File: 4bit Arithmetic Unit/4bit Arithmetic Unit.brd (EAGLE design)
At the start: 162.5 x 108.9 mm, 100 parts

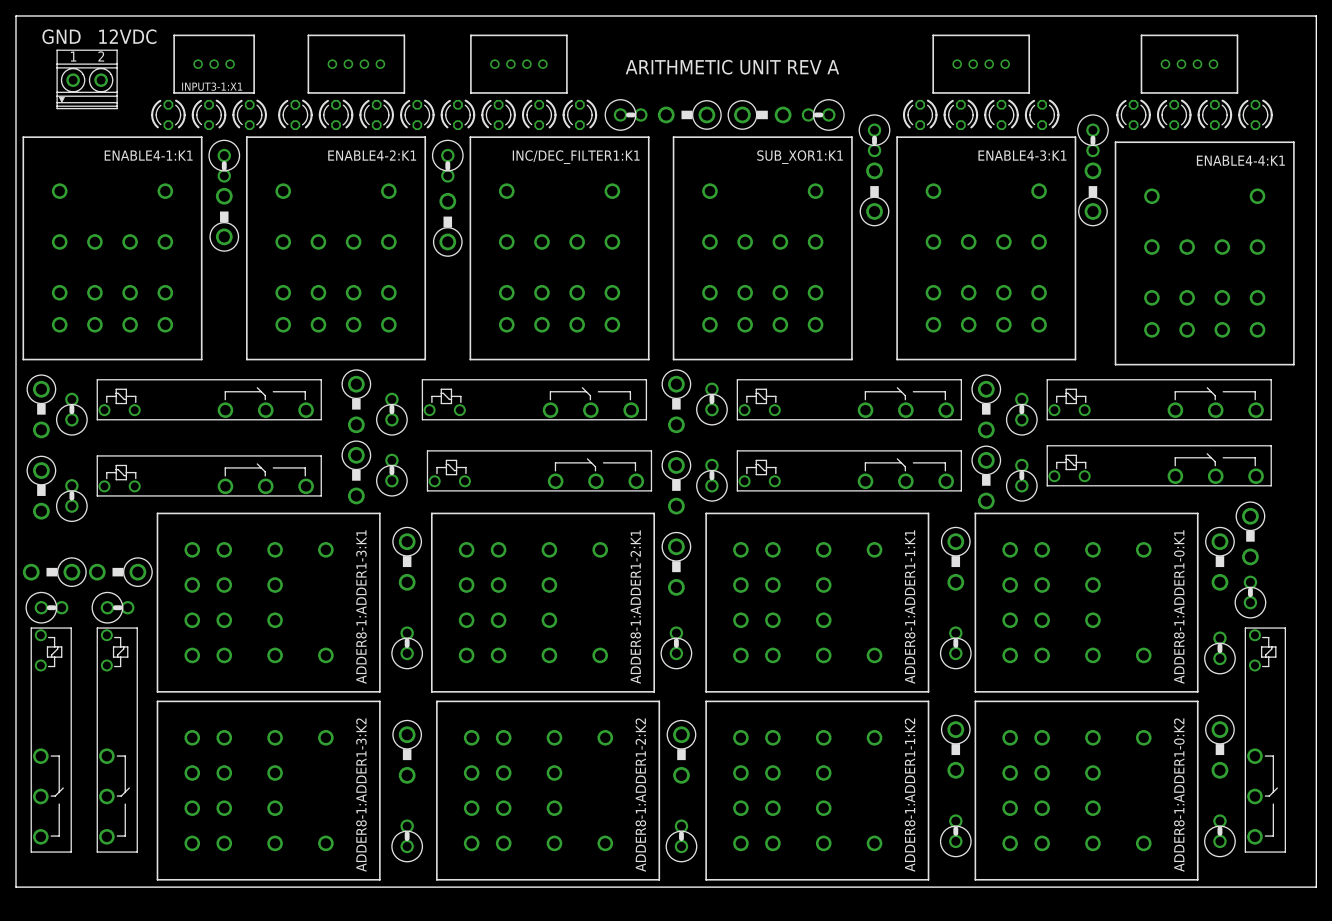
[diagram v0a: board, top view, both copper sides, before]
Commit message: Finishing 4bit AU. Text is actually correct when it appears offset. Worth doing a logical double-check
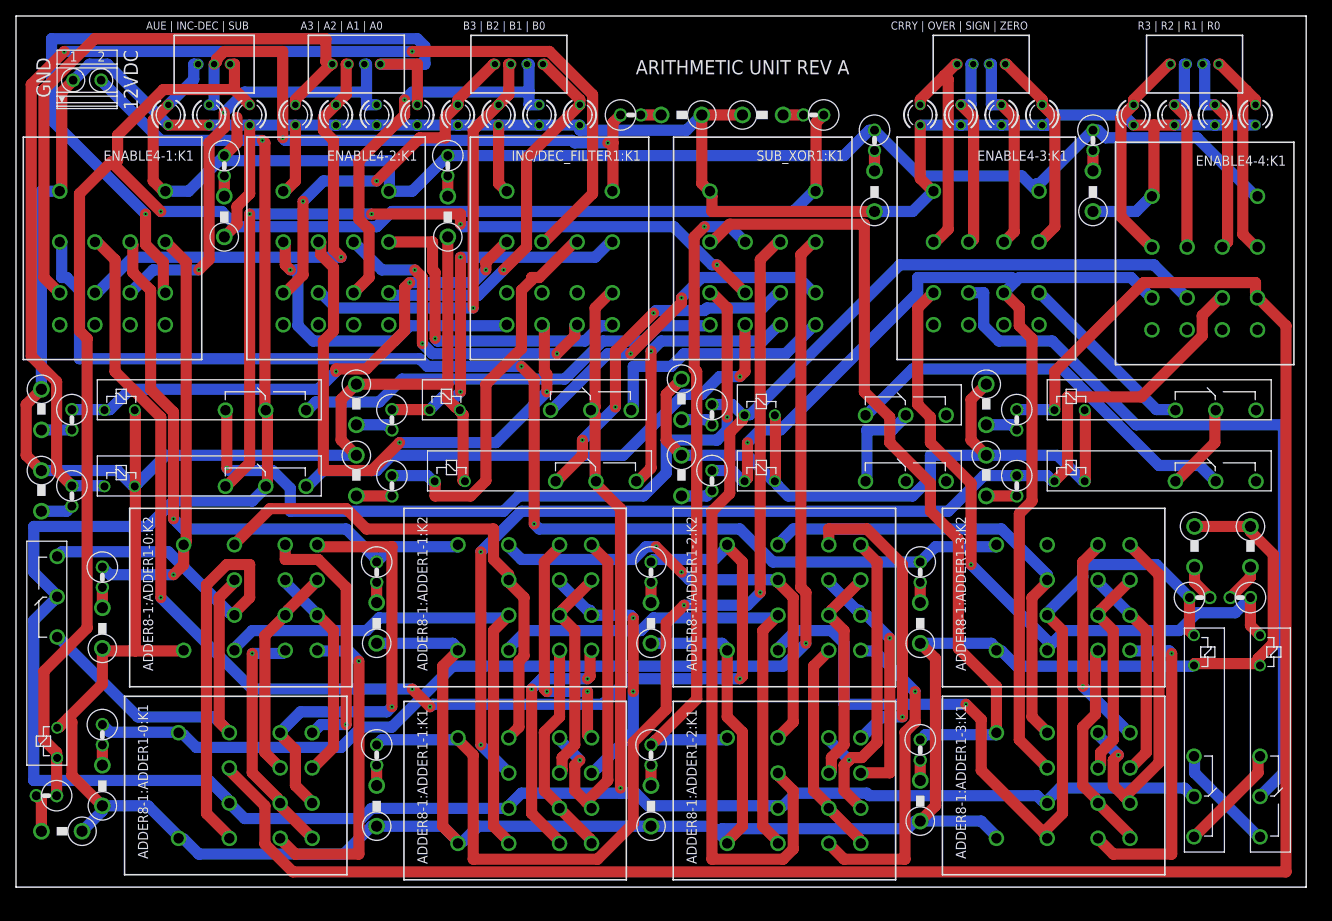
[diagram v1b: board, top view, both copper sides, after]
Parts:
- moved ADDER8-1:D2 153.1 mm to (5.71, 6.99), turned to 180 degrees
- moved ADDER8-1:D1 152.6 mm to (3.81, 11.4), turned to 180 degrees
- moved ADDER8-1:K3 152.4 mm to (154.3, 32.4)
- moved ADDER8-1:D6 149.9 mm to (154.3, 42.5), turned to 270 degrees
- moved ADDER8-1:D5 148.6 mm to (153.0, 36.2), turned to 180 degrees
- moved ADDER8-1:K1 148.3 mm to (6.35, 15.2), turned to 90 degrees
- moved ADDER8-1:ADDER1-0:D3 143.3 mm to (10.8, 38.7), turned to 270 degrees
- moved ADDER8-1:ADDER1-0:D2 142.5 mm to (10.8, 12.7), turned to 90 degrees
- moved ADDER8-1:ADDER1-0:D4 140.5 mm to (10.8, 32.4), turned to 90 degrees
- moved ADDER8-1:ADDER1-0:D1 140.1 mm to (10.8, 19.1), turned to 270 degrees
- moved ADDER8-1:K2 135.9 mm to (146.1, 32.4)
- moved ADDER8-1:D3 135.3 mm to (148.0, 36.2)
- moved ADDER8-1:D4 134.7 mm to (147.3, 42.5), turned to 270 degrees
- moved ADDER8-1:ADDER1-0:K1 122.8 mm to (20.3, 12.7), turned to 270 degrees
- moved ADDER8-1:ADDER1-0:K2 122.4 mm to (21.0, 36.2), turned to 270 degrees
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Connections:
- net AUE: now also INPUT3-1:LED2.A, INPUT3-1:X1.1; no longer INPUT3-1:LED0.A, INPUT3-1:X1.3
- net SUB: now also INPUT3-1:LED0.A, INPUT3-1:X1.3; no longer INPUT3-1:LED2.A, INPUT3-1:X1.1
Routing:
- net GND: track 0.00 -> 738.7 mm
- net +12V: track 0.00 -> 349.7 mm, vias 0 -> 2
- net N$40: track 0.00 -> 254.9 mm
- net SUB: track 0.00 -> 214.6 mm, vias 0 -> 1
- net AUE: track 0.00 -> 181.1 mm
- net N$15: track 0.00 -> 155.8 mm, vias 0 -> 4
- net N$16: track 0.00 -> 152.9 mm, vias 0 -> 2
- net N$19: track 0.00 -> 151.7 mm, vias 0 -> 2
- net N$42: track 0.00 -> 147.6 mm
- net N$24: track 0.00 -> 145.8 mm, vias 0 -> 1
- net N$41: track 0.00 -> 142.2 mm, vias 0 -> 2
- net N$43: track 0.00 -> 136.3 mm, vias 0 -> 1
- net N$23: track 0.00 -> 133.6 mm, vias 0 -> 2
- net ADDER8-1:IN1: track 0.00 -> 111.0 mm, vias 0 -> 1
- net N$1: track 0.00 -> 102.3 mm, vias 0 -> 1
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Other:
- board size 162.5 x 108.9 mm -> 161.3 x 108.9 mm
- board text added: "A3 | A2 | A1 | A0"
- board text added: "AUE | INC-DEC | SUB"
- board text added: "B3 | B2 | B1 | B0"
- board text added: "CRRY | OVER | SIGN | ZERO"
- board text added: "OCTOBER 2017"
- board text added: "R3 | R2 | R1 | R0"

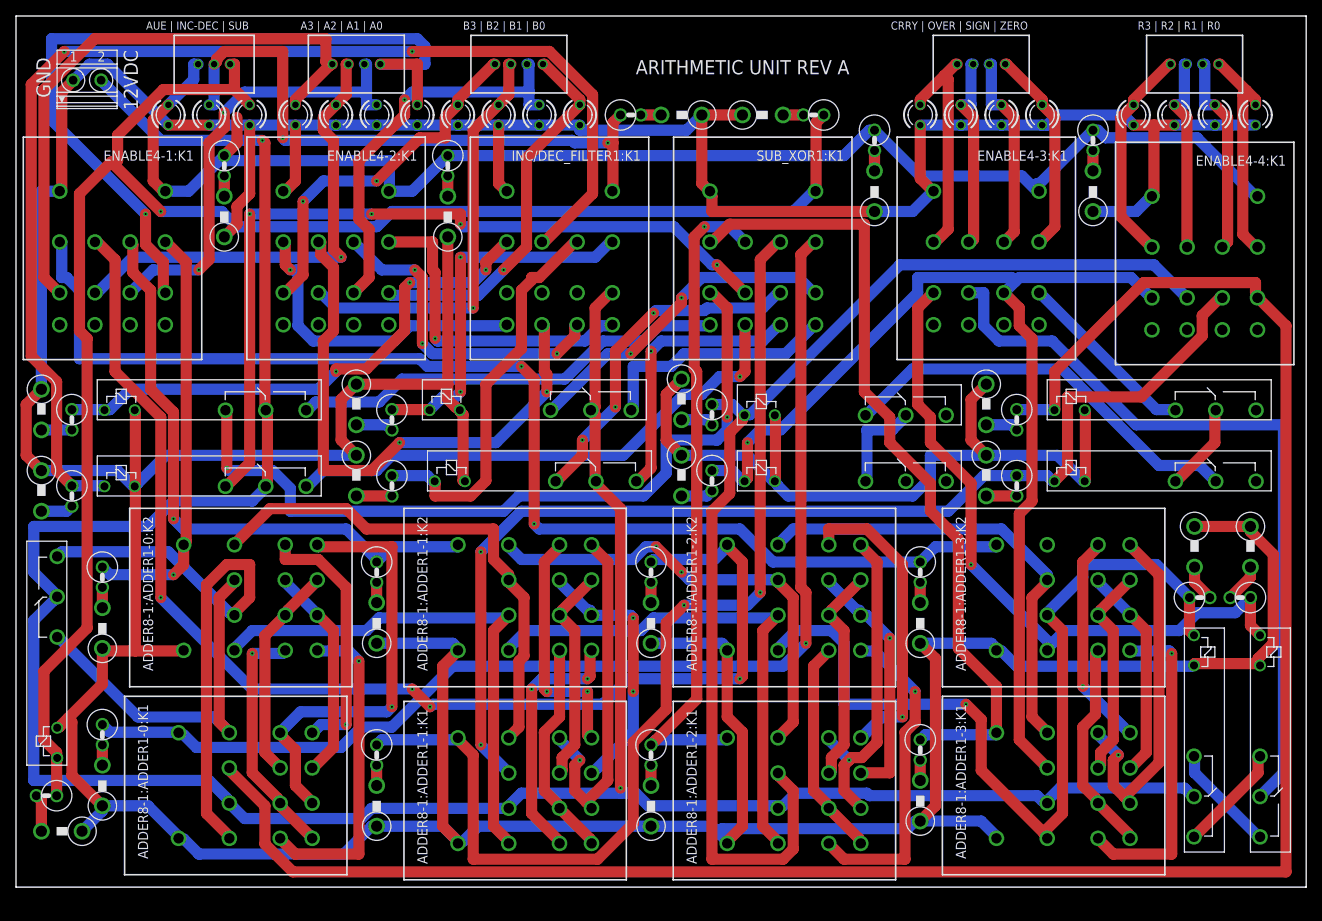
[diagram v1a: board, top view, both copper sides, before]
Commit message: Prettier dual rail adder
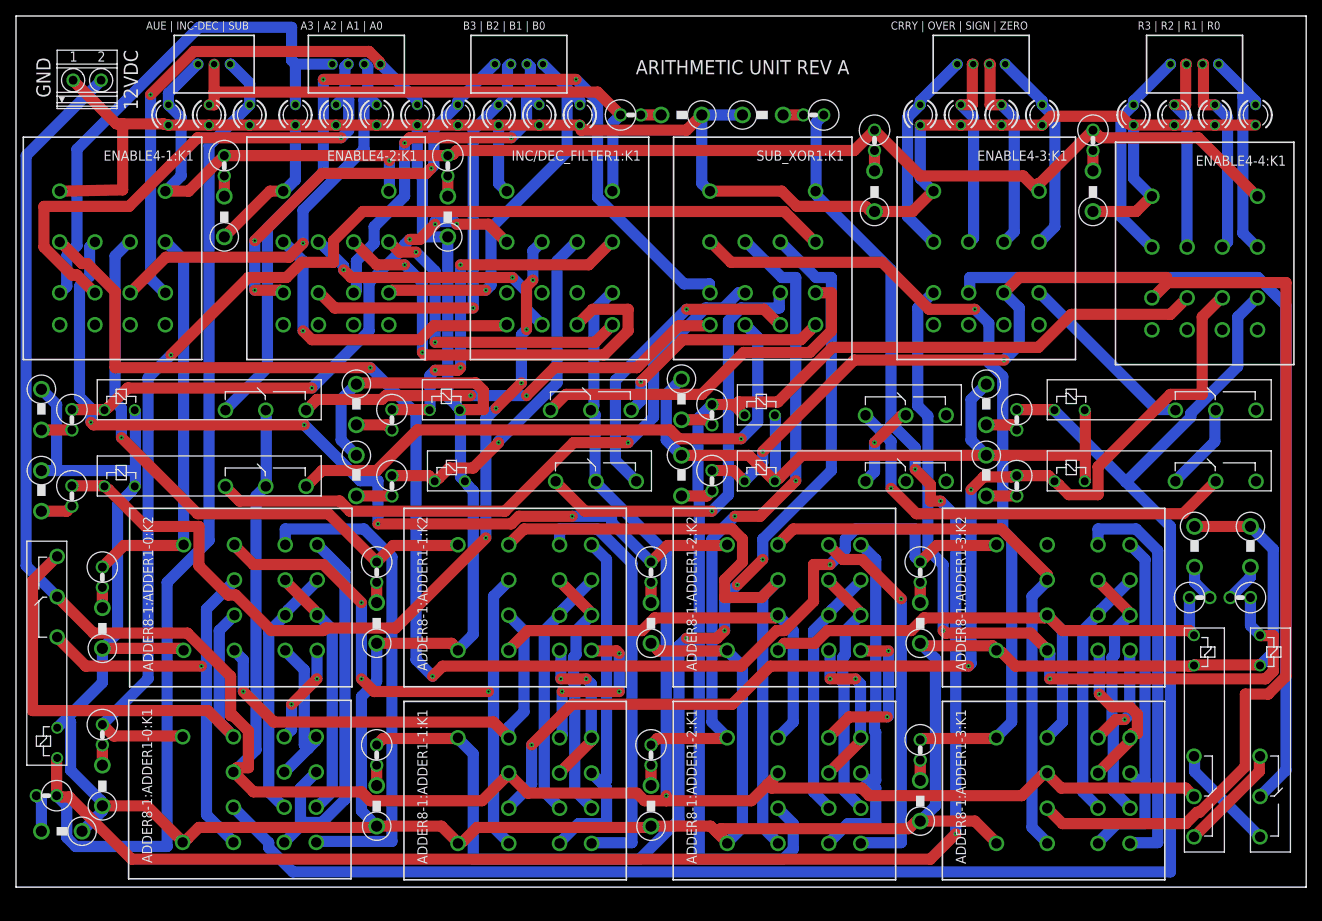
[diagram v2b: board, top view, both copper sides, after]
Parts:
- moved ADDER8-1:ADDER1-0:K1 0.72 mm to (20.8, 12.2)
- moved ADDER8-1:ADDER1-3:K1 0.63 mm to (122.6, 12.1)
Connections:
- net +12V: now also ADDER8-1:ADDER1-0:K1.31, ADDER8-1:ADDER1-1:K1.31, ADDER8-1:ADDER1-2:K1.31, ADDER8-1:ADDER1-3:K1.31; no longer ADDER8-1:ADDER1-0:K1.21, ADDER8-1:ADDER1-1:K1.21, ADDER8-1:ADDER1-2:K1.21, ADDER8-1:ADDER1-3:K1.21
- net ADDER8-1:ADDER1-0:N$1: now also ADDER8-1:ADDER1-0:K2.44; no longer ADDER8-1:ADDER1-0:K1.24, ADDER8-1:ADDER1-0:K2.14
- net ADDER8-1:ADDER1-0:N$2: now also ADDER8-1:ADDER1-0:K1.32, ADDER8-1:ADDER1-0:K2.42; no longer ADDER8-1:ADDER1-0:K2.12
- net ADDER8-1:ADDER1-0:N$3: now also ADDER8-1:ADDER1-0:K1.22; no longer ADDER8-1:ADDER1-0:K1.32
- net ADDER8-1:ADDER1-0:N$4: now also ADDER8-1:ADDER1-0:K1.24; no longer ADDER8-1:ADDER1-0:K1.34
- net ADDER8-1:ADDER1-0:N$5: now also ADDER8-1:ADDER1-0:K1.44, ADDER8-1:ADDER1-0:K2.12; no longer ADDER8-1:ADDER1-0:K1.42, ADDER8-1:ADDER1-0:K2.44
- net ADDER8-1:ADDER1-0:N$6: now also ADDER8-1:ADDER1-0:K1.34, ADDER8-1:ADDER1-0:K1.42, ADDER8-1:ADDER1-0:K2.14; no longer ADDER8-1:ADDER1-0:K1.22, ADDER8-1:ADDER1-0:K1.44, ADDER8-1:ADDER1-0:K2.42
- net ADDER8-1:ADDER1-1:N$1: now also ADDER8-1:ADDER1-1:K2.44; no longer ADDER8-1:ADDER1-1:K1.24, ADDER8-1:ADDER1-1:K2.14
- net ADDER8-1:ADDER1-1:N$2: now also ADDER8-1:ADDER1-1:K1.32, ADDER8-1:ADDER1-1:K2.42; no longer ADDER8-1:ADDER1-1:K2.12
- net ADDER8-1:ADDER1-1:N$3: now also ADDER8-1:ADDER1-1:K1.22; no longer ADDER8-1:ADDER1-1:K1.32
- net ADDER8-1:ADDER1-1:N$4: now also ADDER8-1:ADDER1-1:K1.24; no longer ADDER8-1:ADDER1-1:K1.34
- net ADDER8-1:ADDER1-1:N$5: now also ADDER8-1:ADDER1-1:K1.44, ADDER8-1:ADDER1-1:K2.12; no longer ADDER8-1:ADDER1-1:K1.42, ADDER8-1:ADDER1-1:K2.44
- net ADDER8-1:ADDER1-1:N$6: now also ADDER8-1:ADDER1-1:K1.34, ADDER8-1:ADDER1-1:K1.42, ADDER8-1:ADDER1-1:K2.14; no longer ADDER8-1:ADDER1-1:K1.22, ADDER8-1:ADDER1-1:K1.44, ADDER8-1:ADDER1-1:K2.42
- net ADDER8-1:ADDER1-2:N$1: now also ADDER8-1:ADDER1-2:K2.44; no longer ADDER8-1:ADDER1-2:K1.24, ADDER8-1:ADDER1-2:K2.14
- net ADDER8-1:ADDER1-2:N$2: now also ADDER8-1:ADDER1-2:K1.32, ADDER8-1:ADDER1-2:K2.42; no longer ADDER8-1:ADDER1-2:K2.12
- net ADDER8-1:ADDER1-2:N$3: now also ADDER8-1:ADDER1-2:K1.22; no longer ADDER8-1:ADDER1-2:K1.32
- net ADDER8-1:ADDER1-2:N$4: now also ADDER8-1:ADDER1-2:K1.24; no longer ADDER8-1:ADDER1-2:K1.34
- net ADDER8-1:ADDER1-2:N$5: now also ADDER8-1:ADDER1-2:K1.44, ADDER8-1:ADDER1-2:K2.12; no longer ADDER8-1:ADDER1-2:K1.42, ADDER8-1:ADDER1-2:K2.44
- net ADDER8-1:ADDER1-2:N$6: now also ADDER8-1:ADDER1-2:K1.34, ADDER8-1:ADDER1-2:K1.42, ADDER8-1:ADDER1-2:K2.14; no longer ADDER8-1:ADDER1-2:K1.22, ADDER8-1:ADDER1-2:K1.44, ADDER8-1:ADDER1-2:K2.42
- net ADDER8-1:ADDER1-3:N$1: now also ADDER8-1:ADDER1-3:K2.44; no longer ADDER8-1:ADDER1-3:K1.24, ADDER8-1:ADDER1-3:K2.14
- net ADDER8-1:ADDER1-3:N$2: now also ADDER8-1:ADDER1-3:K1.32, ADDER8-1:ADDER1-3:K2.42; no longer ADDER8-1:ADDER1-3:K2.12
- net ADDER8-1:ADDER1-3:N$3: now also ADDER8-1:ADDER1-3:K1.22; no longer ADDER8-1:ADDER1-3:K1.32
- net ADDER8-1:ADDER1-3:N$4: now also ADDER8-1:ADDER1-3:K1.24; no longer ADDER8-1:ADDER1-3:K1.34
- net ADDER8-1:ADDER1-3:N$5: now also ADDER8-1:ADDER1-3:K1.44, ADDER8-1:ADDER1-3:K2.12; no longer ADDER8-1:ADDER1-3:K1.42, ADDER8-1:ADDER1-3:K2.44
- net ADDER8-1:ADDER1-3:N$6: now also ADDER8-1:ADDER1-3:K1.34, ADDER8-1:ADDER1-3:K1.42, ADDER8-1:ADDER1-3:K2.14; no longer ADDER8-1:ADDER1-3:K1.22, ADDER8-1:ADDER1-3:K1.44, ADDER8-1:ADDER1-3:K2.42
- net ADDER8-1:IN1: now also ADDER8-1:ADDER1-3:K1.41; no longer ADDER8-1:ADDER1-3:K1.11
- net ADDER8-1:N$1: now also ADDER8-1:ADDER1-1:K1.41; no longer ADDER8-1:ADDER1-1:K1.11
- net ADDER8-1:N$2: now also ADDER8-1:ADDER1-1:K1.11; no longer ADDER8-1:ADDER1-1:K1.41
- net ADDER8-1:N$3: now also ADDER8-1:ADDER1-2:K1.41; no longer ADDER8-1:ADDER1-2:K1.11
- net ADDER8-1:N$4: now also ADDER8-1:ADDER1-2:K1.11; no longer ADDER8-1:ADDER1-2:K1.41
- net ADDER8-1:N$6: now also ADDER8-1:ADDER1-3:K1.11; no longer ADDER8-1:ADDER1-3:K1.41
- net ADDER8-1:N$7: now also ADDER8-1:ADDER1-0:K1.11; no longer ADDER8-1:ADDER1-0:K1.41
- net ADDER8-1:N$9: now also ADDER8-1:ADDER1-0:K1.41; no longer ADDER8-1:ADDER1-0:K1.11
- net N$40: now also ADDER8-1:ADDER1-0:K1.21; no longer ADDER8-1:ADDER1-0:K1.31
- net N$41: now also ADDER8-1:ADDER1-1:K1.21; no longer ADDER8-1:ADDER1-1:K1.31
- net N$42: now also ADDER8-1:ADDER1-2:K1.21; no longer ADDER8-1:ADDER1-2:K1.31
- net N$43: now also ADDER8-1:ADDER1-3:K1.21; no longer ADDER8-1:ADDER1-3:K1.31
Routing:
- net SUB: track 214.6 -> 341.8 mm, vias 1 -> 3
- net N$43: track 136.3 -> 186.3 mm, vias 1 -> 2
- net N$19: track 151.7 -> 106.8 mm, vias 2 -> 5
- net N$15: track 155.8 -> 116.1 mm
- net N$1: track 102.3 -> 64.4 mm
- net N$10: track 70.8 -> 33.8 mm
- net N$40: track 254.9 -> 219.2 mm
- net ADDER8-1:ADDER1-0:N$6: track 55.3 -> 19.6 mm, vias 1 -> 0
- net ADDER8-1:IN1: track 111.0 -> 76.8 mm, vias 1 -> 0
- net ADDER8-1:ADDER1-0:N$1: track 30.5 -> 61.8 mm, vias 1 -> 0
- net N$16: track 152.9 -> 179.0 mm, vias 2 -> 3
- net ADDER8-1:ADDER1-1:N$1: track 27.3 -> 52.8 mm
- net ADDER8-1:ADDER1-3:N$6: track 45.7 -> 21.0 mm
- net ADDER8-1:ADDER1-1:N$6: track 45.1 -> 20.5 mm, vias 1 -> 2
- net ADDER8-1:ADDER1-3:N$1: track 26.7 -> 50.6 mm
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
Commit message: Using updated connectors
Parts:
- moved INPUT3-1:LED2 1.02 mm to (20.1, 96.5), flipped to the bottom
- moved INPUT3-1:LED1 0.51 mm to (24.6, 96.5), flipped to the bottom
- moved INPUT3-1:X1 0.25 mm to (24.5, 102.9), turned to 180 degrees
- flipped INPUT3-1:LED0 to the bottom
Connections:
- net CARRY: now also OUTPUT4-2:X1.1; no longer OUTPUT4-2:X1.4
- net N$1: now also INPUT4-1:X1.4; no longer INPUT4-1:X1.1
- net N$2: now also INPUT4-1:X1.3; no longer INPUT4-1:X1.2
- net N$3: now also INPUT4-1:X1.2; no longer INPUT4-1:X1.3
- net N$4: now also INPUT4-1:X1.1; no longer INPUT4-1:X1.4
- net N$5: now also INPUT4-2:X1.4; no longer INPUT4-2:X1.1
- net N$6: now also INPUT4-2:X1.3; no longer INPUT4-2:X1.2
- net N$7: now also INPUT4-2:X1.2; no longer INPUT4-2:X1.3
- net N$8: now also INPUT4-2:X1.1; no longer INPUT4-2:X1.4
- net OVERFLOW: now also OUTPUT4-2:X1.2; no longer OUTPUT4-2:X1.3
- net R0: now also OUTPUT4-1:X1.4; no longer OUTPUT4-1:X1.1
- net R1: now also OUTPUT4-1:X1.3; no longer OUTPUT4-1:X1.2
- net R2: now also OUTPUT4-1:X1.2; no longer OUTPUT4-1:X1.3
- net R3: now also OUTPUT4-1:X1.1; no longer OUTPUT4-1:X1.4
- net SIGN: now also OUTPUT4-2:X1.3; no longer OUTPUT4-2:X1.2
- net ZERO: now also OUTPUT4-2:X1.4; no longer OUTPUT4-2:X1.1
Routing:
- net GND: track 722.2 -> 0.00 mm
- net +12V: track 356.3 -> 0.00 mm, vias 1 -> 0
- net SUB: track 341.8 -> 0.00 mm, vias 3 -> 0
- net N$40: track 219.2 -> 0.00 mm
- net N$43: track 186.3 -> 0.00 mm, vias 2 -> 0
- net N$16: track 179.0 -> 0.00 mm, vias 3 -> 0
- net AUE: track 173.5 -> 0.00 mm, vias 1 -> 0
- net N$24: track 151.6 -> 0.00 mm, vias 1 -> 0
- net N$42: track 142.5 -> 0.00 mm
- net N$41: track 140.9 -> 0.00 mm, vias 3 -> 0
- net N$23: track 140.4 -> 0.00 mm, vias 4 -> 0
- net N$15: track 116.1 -> 0.00 mm, vias 4 -> 0
- net SUB_XOR1:N$7: track 113.5 -> 0.00 mm, vias 2 -> 0
- net N$19: track 106.8 -> 0.00 mm, vias 5 -> 0
- net N$44: track 105.7 -> 0.00 mm
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
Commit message: Minor formatting changes
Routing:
- net GND: track 0.00 -> 722.6 mm
- net +12V: track 0.00 -> 318.5 mm
- net AUE: track 0.00 -> 272.4 mm
- net N$40: track 0.00 -> 251.7 mm, vias 0 -> 1
- net N$42: track 0.00 -> 221.6 mm, vias 0 -> 1
- net N$15: track 0.00 -> 220.4 mm, vias 0 -> 7
- net N$16: track 0.00 -> 216.1 mm, vias 0 -> 2
- net SUB: track 0.00 -> 204.9 mm, vias 0 -> 1
- net N$24: track 0.00 -> 176.1 mm, vias 0 -> 4
- net N$41: track 0.00 -> 157.9 mm
- net N$23: track 0.00 -> 133.1 mm, vias 0 -> 6
- net N$19: track 0.00 -> 130.7 mm, vias 0 -> 4
- net N$43: track 0.00 -> 125.4 mm, vias 0 -> 3
- net N$25: track 0.00 -> 111.4 mm, vias 0 -> 3
- net SUB_XOR1:N$7: track 0.00 -> 103.5 mm, vias 0 -> 4
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- added copper zone on layer 1, net +12V
- added copper zone on layer 16, net GND
